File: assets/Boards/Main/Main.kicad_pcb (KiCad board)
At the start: 2 copper layers, 69.9 x 29.2 mm, 9 parts, among them J1 PWR, J2 CTRLS_BOARD, U1 DFRobot_MAX98357, U2 Waveshare_ESP32-S3-Tiny

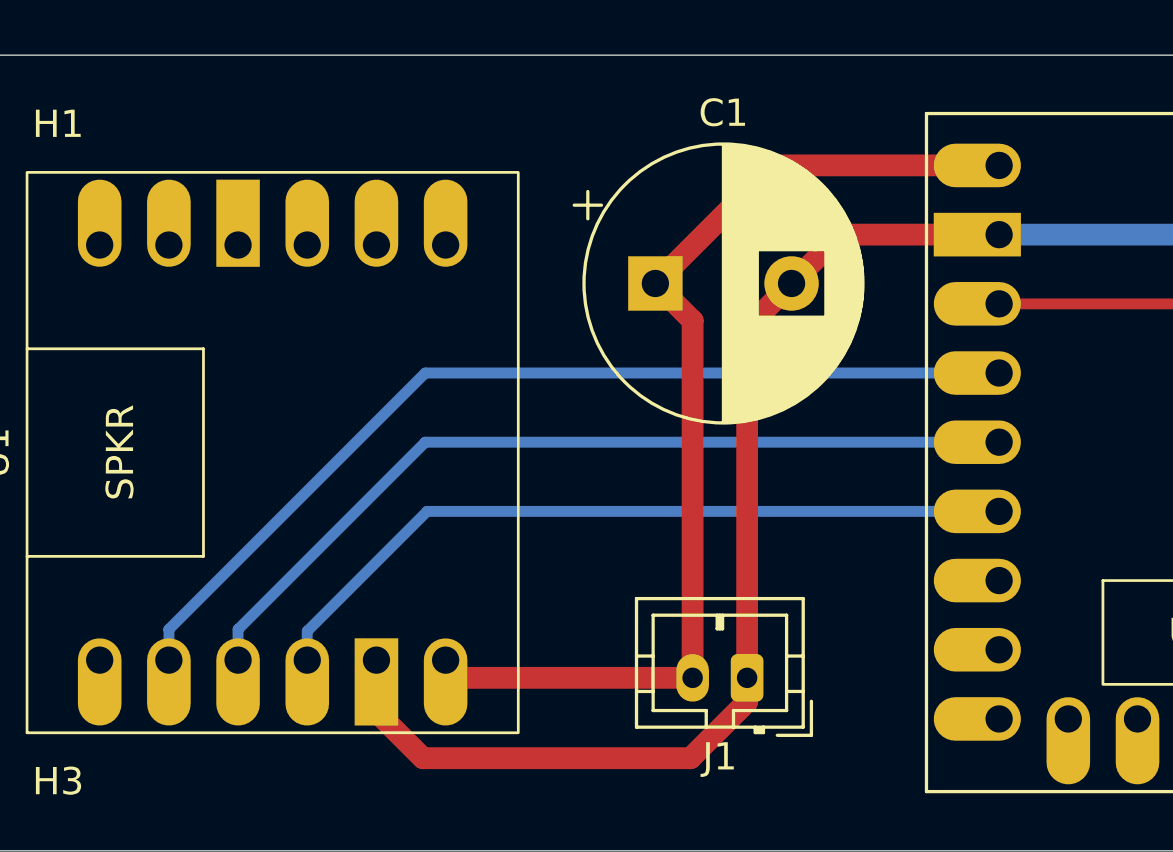
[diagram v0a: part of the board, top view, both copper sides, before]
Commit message: Rotated capacitor.
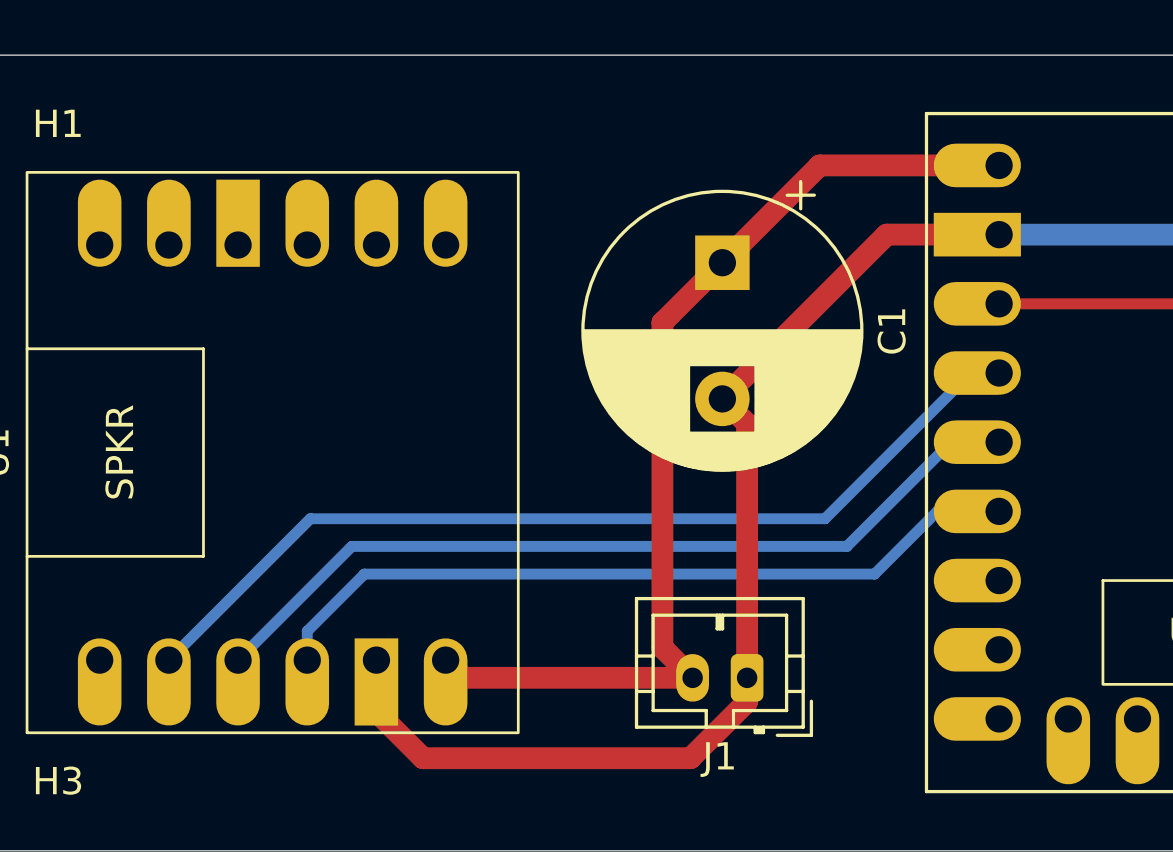
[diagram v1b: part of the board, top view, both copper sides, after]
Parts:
- moved C1 2.58 mm to (148.6, 59.7), turned to -90 degrees
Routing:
- net /5V: track 38.8 -> 37.6 mm
- net Net-(U1-DIN): track 35.5 -> 34.8 mm
- net Net-(U1-BCLK): track 31.9 -> 31.3 mm

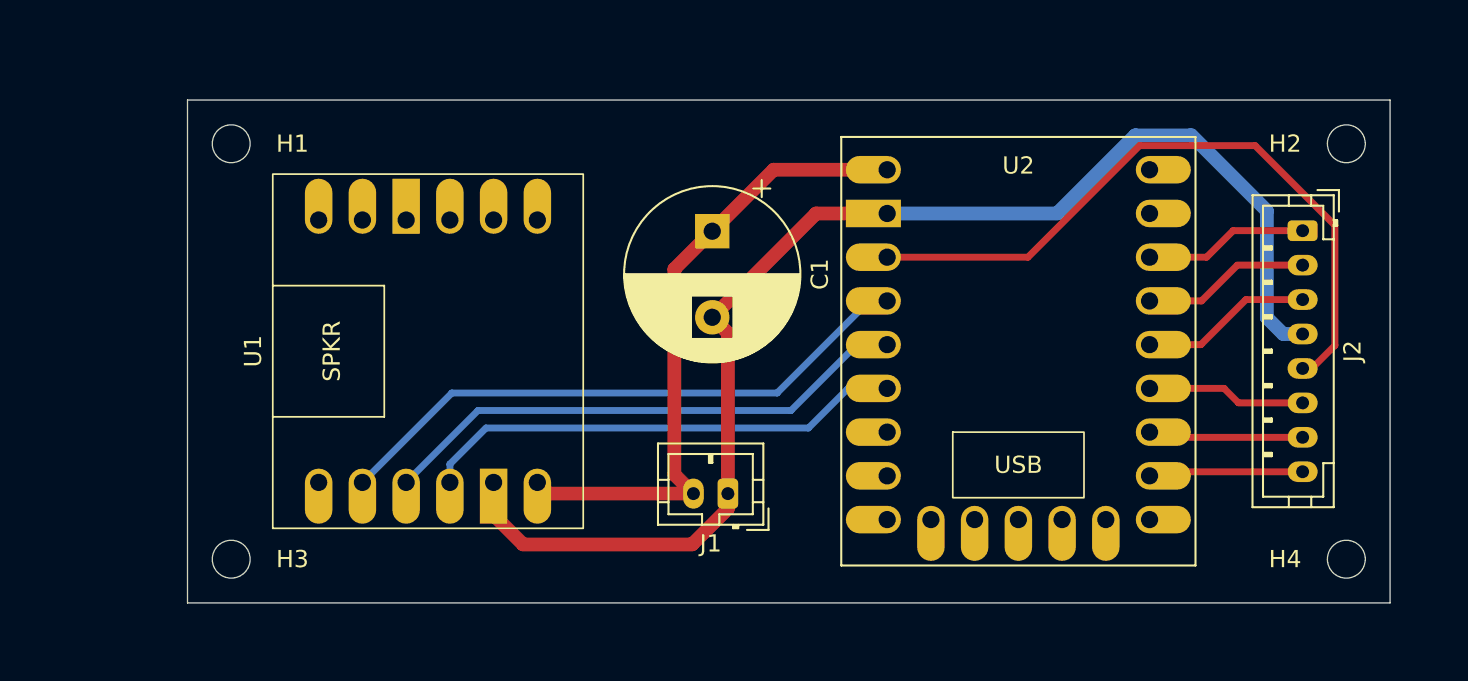
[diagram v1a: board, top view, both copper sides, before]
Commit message: Added ground plane, RF shield soldering points and text.
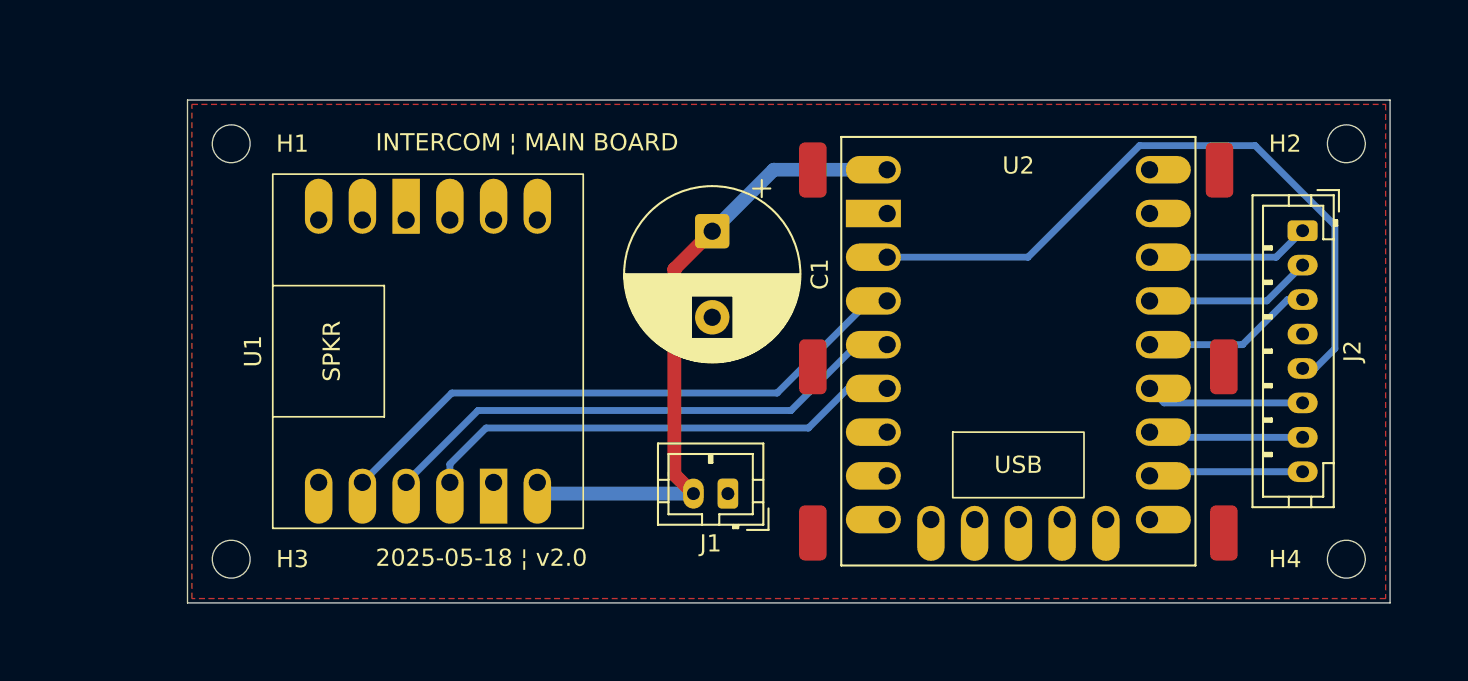
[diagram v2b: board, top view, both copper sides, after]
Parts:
- added U3: ~, Custom Footprints:Solder pad 1.6x3.3mm, F.Cu at (154.4, 77.2)
- added U4: ~, Custom Footprints:Solder pad 1.6x3.3mm, F.Cu at (178.3, 77.2)
- added U5: ~, Custom Footprints:Solder pad 1.6x3.3mm, F.Cu at (178.1, 56.1)
- added U6: ~, Custom Footprints:Solder pad 1.6x3.3mm, F.Cu at (154.4, 56.1)
- added U7: ~, Custom Footprints:Solder pad 1.6x3.3mm, F.Cu at (178.3, 67.6)
- added U8: ~, Custom Footprints:Solder pad 1.6x3.3mm, F.Cu at (154.4, 67.6)
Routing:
- net /GND: track 75.6 -> 1.89 mm
- net /3V3: track 40.0 -> 40.7 mm
- added copper zone on F.Cu, net /GND
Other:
- board text added: "2025-05-18 ¦ v2.0"
- board text added: "INTERCOM ¦ MAIN BOARD"

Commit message: Reworked boards.
Added LDO for the mic. Changed layout of the main board to move the cap out of the way. Added ground and power plane. Added R33's for the signal lines of the mic.
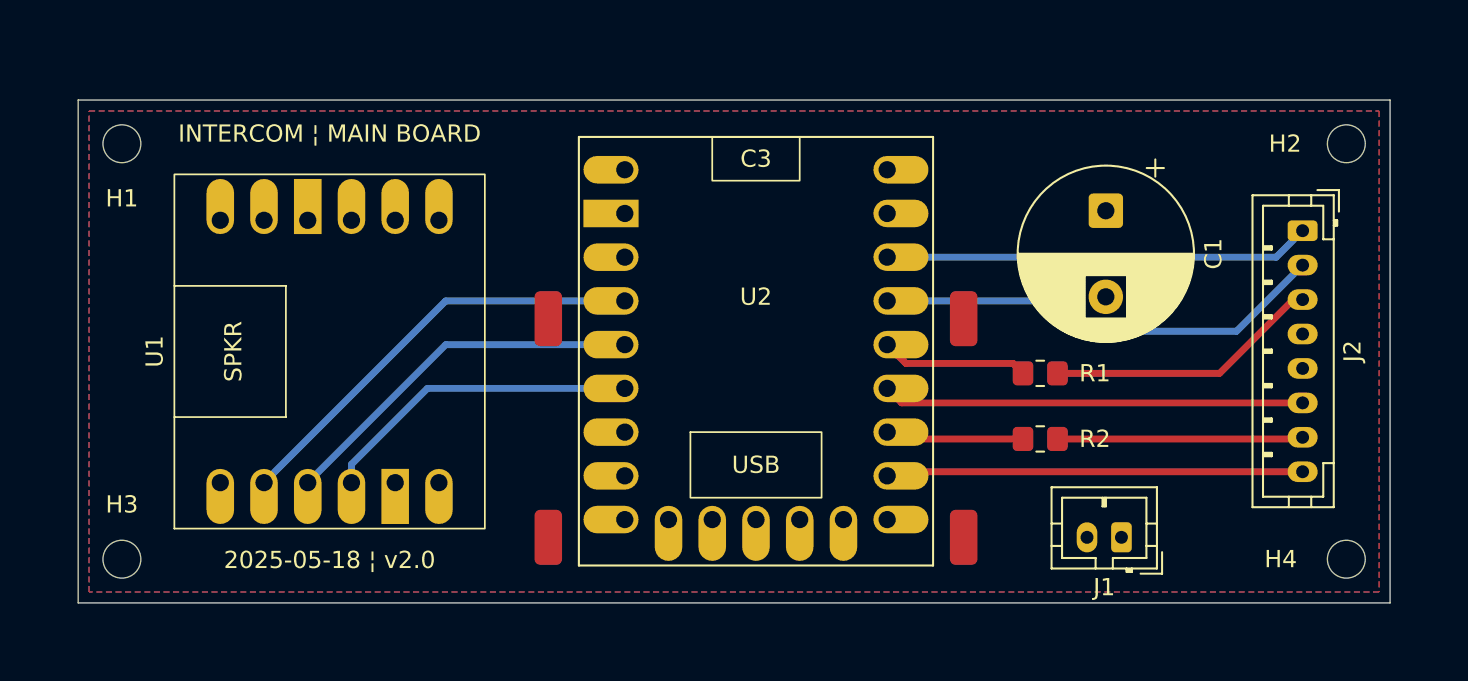
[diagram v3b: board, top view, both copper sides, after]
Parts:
- removed U6, U7: ~, Custom Footprints:Solder pad 1.6x3.3mm
- added R1: 33, Resistor_SMD:R_0805_2012Metric_Pad1.20x1.40mm_HandSolder, F.Cu at (167.6, 67.9)
- added R2: 33, Resistor_SMD:R_0805_2012Metric_Pad1.20x1.40mm_HandSolder, F.Cu at (167.6, 71.8)
- moved J1 23.0 mm to (172.4, 77.5)
- moved C1 22.9 mm to (171.4, 58.5)
- moved U5 17.2 mm to (163.2, 64.8)
- moved U8 15.6 mm to (139.1, 64.8)
- moved U3 15.4 mm to (139.1, 77.5)
- moved U2 15.2 mm to (143.5, 56.1)
- moved U4 15.1 mm to (163.2, 77.5)
- moved H1 6.35 mm to (114.3, 54.6)
- moved H3 6.35 mm to (114.3, 78.7)
- moved U1 5.72 mm to (135.3, 66.7)
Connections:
- net /GND renamed GND
- net Net-(J2-Pin_1) renamed LG
- net Net-(J2-Pin_2) renamed LR
- net Net-(J2-Pin_6) renamed MICROPHONE_DATA
- net Net-(J2-Pin_8) renamed PB
- net Net-(U1-BCLK) renamed SPEAKER_SCK
- net Net-(U1-DIN) renamed SPEAKER_DATA
- net Net-(U1-LRC) renamed SPEAKER_WS
- C1 pad 1: /5V -> +5V
- J1 pad 2: /5V -> +5V
- J2 pad 3: Net-(J2-Pin_3) -> MICROPHONE_SCK
- J2 pad 5: /3V3 -> +5V
- J2 pad 7: Net-(J2-Pin_7) -> MICROPHONE_WS
- U1 pad 6: /5V -> +5V
- U2 pad 1: /5V -> +5V
- U2 pad 17: Net-(J2-Pin_7) -> Net-(U2-14)
- U2 pad 19: Net-(J2-Pin_3) -> Net-(U2-16)
- U2 pad 3: /3V3 -> unconnected-(U2-3V3-Pad3)
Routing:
- net /3V3: track 40.7 -> 0.00 mm
- net /5V: track 37.6 -> 0.00 mm
- net LR: track 9.75 -> 26.5 mm
- net MICROPHONE_SCK: track 0.00 -> 16.0 mm
- net LG: track 9.53 -> 24.8 mm
- net MICROPHONE_DATA: track 9.24 -> 24.5 mm
- net PB: track 9.33 -> 24.2 mm
- net MICROPHONE_WS: track 0.00 -> 14.3 mm
- net Net-(J2-Pin_3): track 9.97 -> 0.00 mm
- net SPEAKER_WS: track 28.3 -> 18.8 mm
- net SPEAKER_SCK: track 31.3 -> 21.7 mm
- net SPEAKER_DATA: track 34.8 -> 25.3 mm
- net Net-(J2-Pin_7): track 9.44 -> 0.00 mm
- net Net-(U2-16): track 0.00 -> 8.58 mm
- net Net-(U2-14): track 0.00 -> 8.05 mm
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- added copper zone on B.Cu, net +5V
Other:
- board size 69.9 x 29.2 mm -> 76.2 x 29.2 mm

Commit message: Fixed ERC errors. Switched to double ground plane instead of ground and power plane. Switched to 1uF caps for the LDO conforming to the data sheet. Added logo.
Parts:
- added G***: LOGO, Custom Footprints:Eletronica Logo, F.Cu at (174.7, 70.1)
- moved C1 4.32 mm to (171.4, 62.8), turned to 90 degrees
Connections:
- J2 pad 1: LG -> GND
- J2 pad 2: LR -> +5V
- J2 pad 3: MICROPHONE_SCK -> LG
- J2 pad 4: GND -> LR
- J2 pad 5: +5V -> MICROPHONE_SCK
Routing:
- net +5V: track 0.00 -> 92.5 mm
- net GND: track 0.00 -> 8.73 mm, vias 0 -> 2
- net MICROPHONE_SCK: track 16.0 -> 14.4 mm
- net LR: track 26.5 -> 25.9 mm
- added copper zone on B.Cu, net GND
- removed copper zone on B.Cu, net +5V

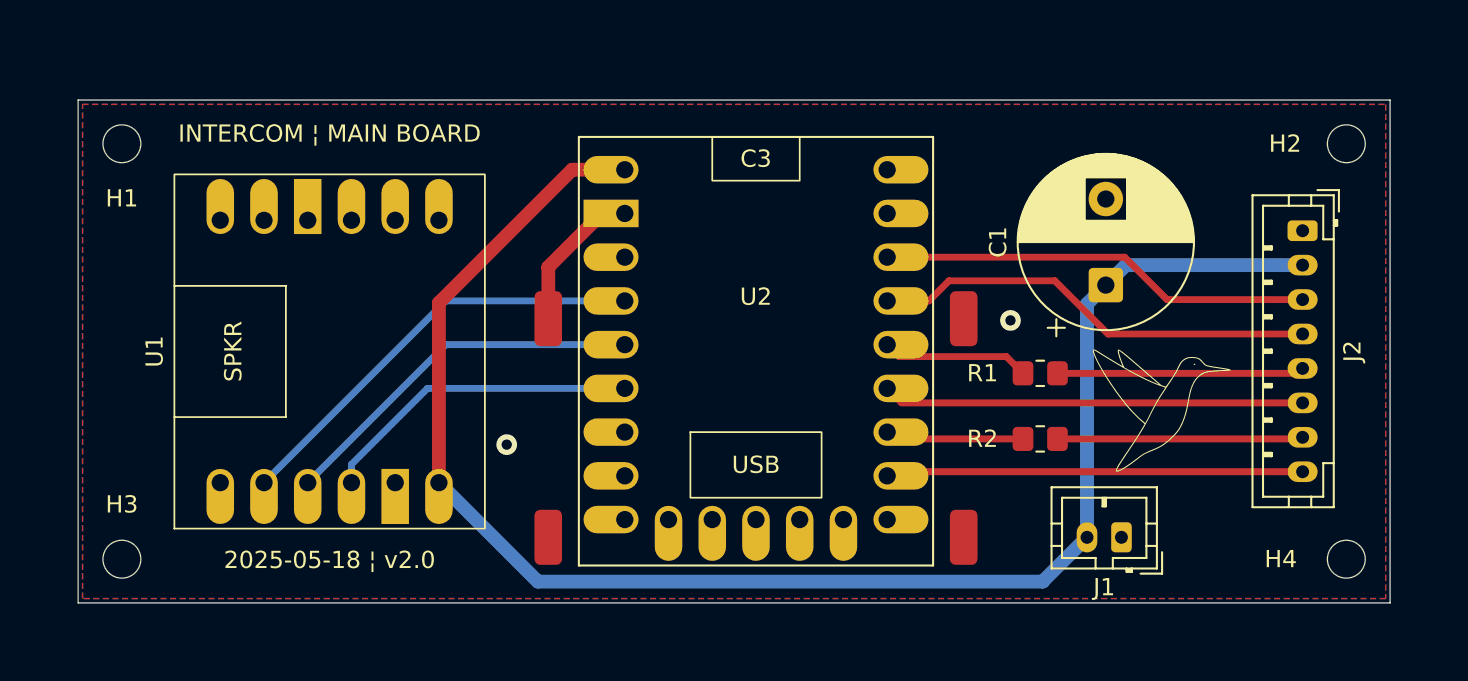
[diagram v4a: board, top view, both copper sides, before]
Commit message: Applied suggestions from Rick Hartley.
See https://www.youtube.com/watch?v=ySuUZEjARPY.
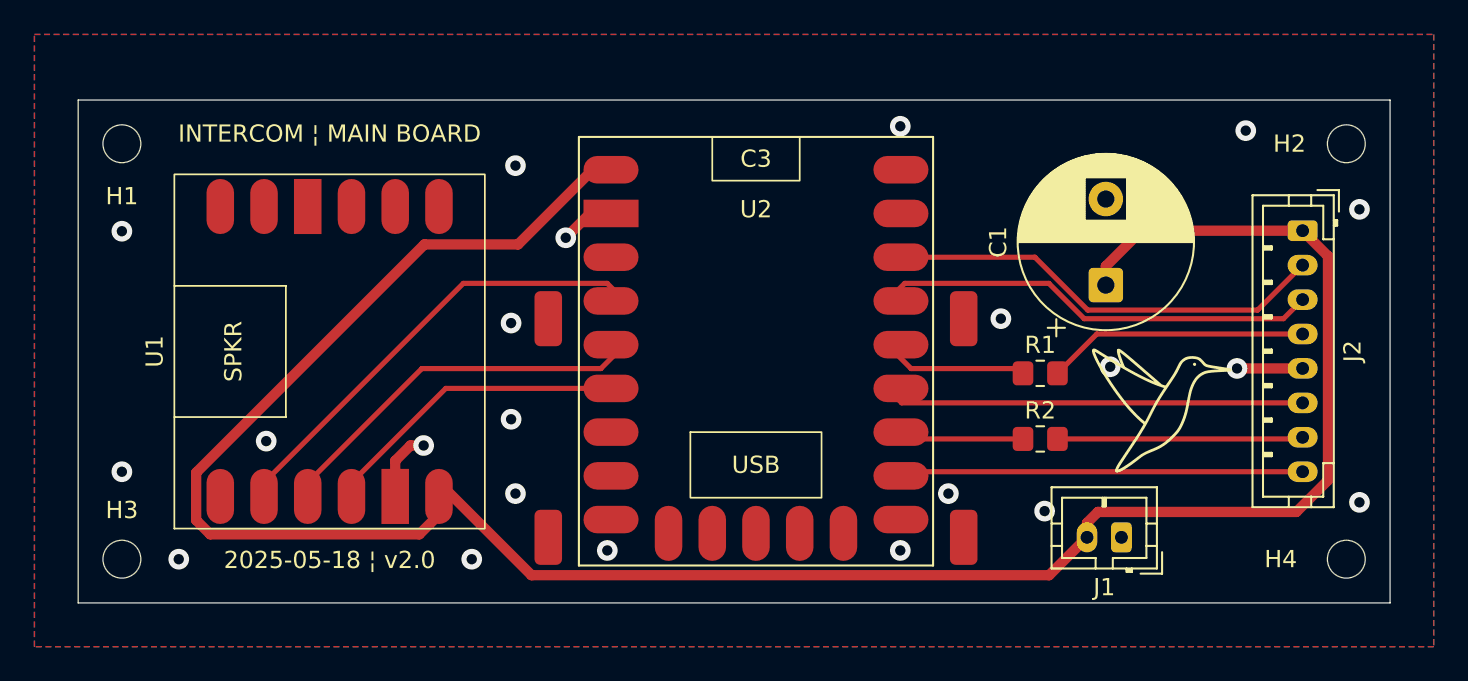
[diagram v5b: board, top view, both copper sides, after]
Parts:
- U1: footprint Custom Footprints:DFRobot_MAX98357 -> Custom Footprints:DFRobot_MAX98357_SMD
- U2: footprint Custom Footprints:Waveshare_ESP32-S3-Tiny -> Custom Footprints:Waveshare_ESP32-S3-Tiny_SMD
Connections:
- J2 pad 1: GND -> +5V
- J2 pad 2: +5V -> LG
- J2 pad 3: LG -> LR
- J2 pad 4: LR -> MICROPHONE_SCK
- J2 pad 5: MICROPHONE_SCK -> GND
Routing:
- net +5V: track 92.5 -> 136.9 mm
- net GND: track 8.73 -> 11.2 mm, vias 2 -> 22
- net LG: track 25.1 -> 26.5 mm
- net SPEAKER_DATA: track 25.3 -> 26.2 mm
- net MICROPHONE_SCK: track 14.4 -> 15.2 mm
- net LR: track 25.9 -> 26.6 mm
- net SPEAKER_WS: track 18.8 -> 18.1 mm

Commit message: Applied suggestions from people from the KiCad forum.
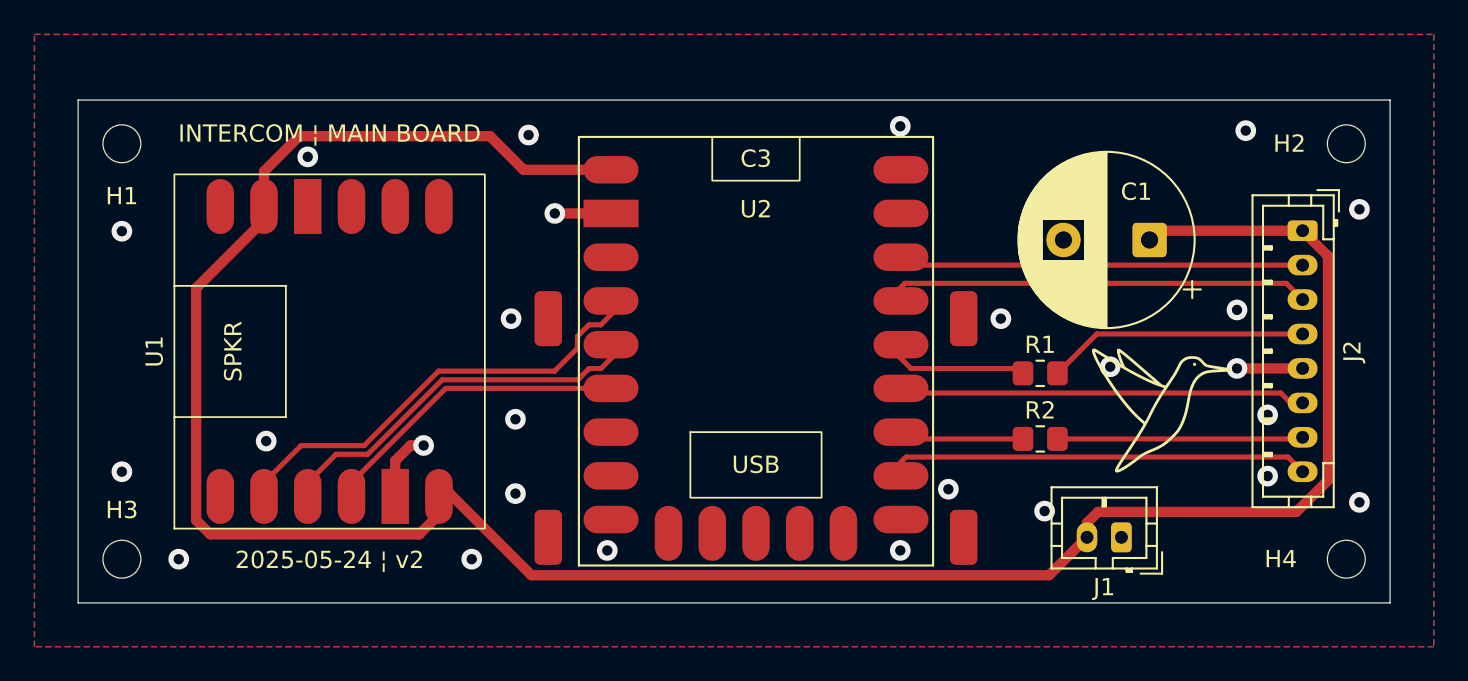
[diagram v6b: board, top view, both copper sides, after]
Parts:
- moved C1 3.65 mm to (174.0, 60.2), turned to 180 degrees
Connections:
- U1 pad 10: unconnected-(U1-GND2-Pad10) -> GND
- U1 pad 11: unconnected-(U1-VCC2-Pad11) -> +5V
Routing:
- net +5V: track 136.9 -> 142.2 mm
- net LG: track 26.5 -> 24.3 mm
- net LR: track 26.6 -> 24.9 mm
- net PB: track 24.2 -> 24.9 mm
- net GND: track 11.2 -> 11.3 mm, vias 22 -> 26
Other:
- board text added: "2025-05-24 ¦ v2"
- board text removed: "2025-05-18 ¦ v2.0"
